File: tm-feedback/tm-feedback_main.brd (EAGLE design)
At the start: 100 x 80 mm, 38 parts

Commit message: Started on PIC schematic
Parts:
- added MICROCONTROLLER1:C2, MICROCONTROLLER1:C4, MICROCONTROLLER1:C5: 0.1uF, rcl:C0805
- added MICROCONTROLLER1:C3: 10uF, rcl:C0805
- added MICROCONTROLLER1:C6, MICROCONTROLLER1:C7: 27pF, rcl:C0805
- added MICROCONTROLLER1:LED2, MICROCONTROLLER1:LED3, MICROCONTROLLER1:LED4: (no value), led:CHIPLED_0805
- added MICROCONTROLLER1:R2, MICROCONTROLLER1:R3, MICROCONTROLLER1:R4, MICROCONTROLLER1:R5, MICROCONTROLLER1:R6: (no value), resistor:R0805
- added MICROCONTROLLER1:SJ1: (no value), jumper:SJ
- added MICROCONTROLLER1:U2: MCRSD20000F183000RR, tactile-music:CRYSTAL-FOOTPRINT
- moved MICROCONTROLLER1:LED1 289.0 mm to (-92.7, -359.4)
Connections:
- removed net MICROCONTROLLER1:AVDD: MICROCONTROLLER1:U1.17
- removed net MICROCONTROLLER1:AVSS: MICROCONTROLLER1:U1.16
- removed net MICROCONTROLLER1:VSS: MICROCONTROLLER1:U1.6
- new net MICROCONTROLLER1:!MCLR: MICROCONTROLLER1:JP1.6, MICROCONTROLLER1:R1.1, MICROCONTROLLER1:R2.1, MICROCONTROLLER1:SJ1.1
- new net MICROCONTROLLER1:LED1: MICROCONTROLLER1:R6.2
- new net MICROCONTROLLER1:LED2: MICROCONTROLLER1:R3.2
- new net MICROCONTROLLER1:LED3: MICROCONTROLLER1:R4.2
- new net MICROCONTROLLER1:LED4: MICROCONTROLLER1:R5.2
- new net MICROCONTROLLER1:N$1: MICROCONTROLLER1:R1.2, MICROCONTROLLER1:U1.18
- new net MICROCONTROLLER1:N$10: MICROCONTROLLER1:LED1.A, MICROCONTROLLER1:R6.1
- new net MICROCONTROLLER1:N$2: MICROCONTROLLER1:C1.1, MICROCONTROLLER1:SJ1.2
- new net MICROCONTROLLER1:N$3: MICROCONTROLLER1:C3.1, MICROCONTROLLER1:U1.7
- new net MICROCONTROLLER1:N$4: MICROCONTROLLER1:LED2.A, MICROCONTROLLER1:R3.1
- new net MICROCONTROLLER1:N$6: MICROCONTROLLER1:LED3.A, MICROCONTROLLER1:R4.1
- new net MICROCONTROLLER1:N$8: MICROCONTROLLER1:LED4.A, MICROCONTROLLER1:R5.1
- new net MICROCONTROLLER1:OSC1: MICROCONTROLLER1:C6.1, MICROCONTROLLER1:U1.30, MICROCONTROLLER1:U2.1
- new net MICROCONTROLLER1:OSC2: MICROCONTROLLER1:C7.1, MICROCONTROLLER1:U1.31, MICROCONTROLLER1:U2.2
- new net MICROCONTROLLER1:PGC: MICROCONTROLLER1:JP1.2
- new net MICROCONTROLLER1:PGD: MICROCONTROLLER1:JP1.3
- net D_3V3: now also MICROCONTROLLER1:C2.1, MICROCONTROLLER1:C4.1, MICROCONTROLLER1:C5.1, MICROCONTROLLER1:JP1.5, MICROCONTROLLER1:R2.2, MICROCONTROLLER1:U1.17, MICROCONTROLLER1:U1.28, MICROCONTROLLER1:U1.40
- net D_GND: now also MICROCONTROLLER1:C1.2, MICROCONTROLLER1:C2.2, MICROCONTROLLER1:C3.2, MICROCONTROLLER1:C4.2, MICROCONTROLLER1:C5.2, MICROCONTROLLER1:C6.2, MICROCONTROLLER1:C7.2, MICROCONTROLLER1:JP1.4, MICROCONTROLLER1:LED1.C, MICROCONTROLLER1:LED2.C, MICROCONTROLLER1:LED3.C, MICROCONTROLLER1:LED4.C, MICROCONTROLLER1:U1.16, MICROCONTROLLER1:U1.29, MICROCONTROLLER1:U1.39, MICROCONTROLLER1:U1.6

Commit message: Change PS, add button, remove MOTOR_DRIVER
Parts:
- removed MOTOR_DRIVER1:JP1, MOTOR_DRIVER2:JP1: (no value), jumper:JP1
- removed MOTOR_DRIVER1:LED1, MOTOR_DRIVER2:LED1: (no value), led:CHIPLED_0805
- removed MOTOR_DRIVER1:MOTOR, MOTOR_DRIVER2:MOTOR: JST-SMD-2, tactile-music:JST-SMD-2
- removed MOTOR_DRIVER1:R1, MOTOR_DRIVER2:R1: 10k, rcl:R0805
- removed MOTOR_DRIVER1:R2, MOTOR_DRIVER2:R2: (no value), rcl:R0805
- removed MOTOR_DRIVER1:U$1, MOTOR_DRIVER2:U$1: PMF370XN, tactile-music:SOT323(SC-70)
- removed MOTOR_DRIVER1:U$2, MOTOR_DRIVER2:U$2: DB2S308, tactile-music:SOD-523
- removed POWER_SUPPLY1:U$2: MCP1824T-3302E/OT, tactile-music:SOT95P270X145-5N
- added MOTOR_DRIVERS, OFF-BOARD_POWER, POWER_SUPPLY1:BATTERY: JST-SMD-2, tactile-music:JST-SMD-2
- added POWER_SUPPLY1:C1, POWER_SUPPLY1:C2: (no value), rcl:C0805
- added POWER_SUPPLY1:R2: 60, resistor:R0805
- added POWER_SUPPLY1:U$3: PMF370XN, tactile-music:SOT323(SC-70)
- POWER_SUPPLY1:R1: value (none) -> 60
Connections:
- removed net A_3V3: MOTOR_DRIVER1:JP1.1, MOTOR_DRIVER1:MOTOR.1, MOTOR_DRIVER1:U$2.1, MOTOR_DRIVER2:JP1.1, MOTOR_DRIVER2:MOTOR.1, MOTOR_DRIVER2:U$2.1
- removed net A_GND: MOTOR_DRIVER1:R1.1, MOTOR_DRIVER1:U$1.2, MOTOR_DRIVER2:R1.1, MOTOR_DRIVER2:U$1.2
- removed net BUTTON1:VCC: BUTTON1:U1.5
- removed net D_3V3: BLUETOOTH1:C1.1, BLUETOOTH1:U$1.23, MICROCONTROLLER1:C2.1, MICROCONTROLLER1:C4.1, MICROCONTROLLER1:C5.1, MICROCONTROLLER1:JP1.5, MICROCONTROLLER1:R2.2, MICROCONTROLLER1:U1.17, MICROCONTROLLER1:U1.28, MICROCONTROLLER1:U1.40
- removed net D_GND: BLUETOOTH1:C1.2, BLUETOOTH1:LED1.C, BLUETOOTH1:LED2.C, BLUETOOTH1:LED3.C, BLUETOOTH1:R2.1, BLUETOOTH1:U$1.1, BLUETOOTH1:U$1.16, BLUETOOTH1:U$1.24, BLUETOOTH1:U$1.9, MICROCONTROLLER1:C1.2, MICROCONTROLLER1:C2.2, MICROCONTROLLER1:C3.2, MICROCONTROLLER1:C4.2, MICROCONTROLLER1:C5.2, MICROCONTROLLER1:C6.2, MICROCONTROLLER1:C7.2, MICROCONTROLLER1:JP1.4, MICROCONTROLLER1:LED1.C, MICROCONTROLLER1:LED2.C, MICROCONTROLLER1:LED3.C, MICROCONTROLLER1:LED4.C, MICROCONTROLLER1:U1.16, MICROCONTROLLER1:U1.29, MICROCONTROLLER1:U1.39, MICROCONTROLLER1:U1.6
- removed net MOTOR_DRIVER1:N$1: MOTOR_DRIVER1:MOTOR.2, MOTOR_DRIVER1:R2.1, MOTOR_DRIVER1:U$1.3, MOTOR_DRIVER1:U$2.2
- removed net MOTOR_DRIVER1:N$2: MOTOR_DRIVER1:JP1.2, MOTOR_DRIVER1:LED1.A
- removed net MOTOR_DRIVER1:N$3: MOTOR_DRIVER1:LED1.C, MOTOR_DRIVER1:R2.2
- removed net MOTOR_DRIVER2:N$1: MOTOR_DRIVER2:MOTOR.2, MOTOR_DRIVER2:R2.1, MOTOR_DRIVER2:U$1.3, MOTOR_DRIVER2:U$2.2
- removed net MOTOR_DRIVER2:N$2: MOTOR_DRIVER2:JP1.2, MOTOR_DRIVER2:LED1.A
- removed net MOTOR_DRIVER2:N$3: MOTOR_DRIVER2:LED1.C, MOTOR_DRIVER2:R2.2
- removed net N$15: MOTOR_DRIVER1:R1.2, MOTOR_DRIVER1:U$1.1
- removed net N$16: MOTOR_DRIVER2:R1.2, MOTOR_DRIVER2:U$1.1
- new net +3V3: BLUETOOTH1:C1.1, BLUETOOTH1:U$1.23, MICROCONTROLLER1:C2.1, MICROCONTROLLER1:C4.1, MICROCONTROLLER1:C5.1, MICROCONTROLLER1:JP1.5, MICROCONTROLLER1:R2.2, MICROCONTROLLER1:U1.17, MICROCONTROLLER1:U1.28, MICROCONTROLLER1:U1.40, POWER_SUPPLY1:C2.2, POWER_SUPPLY1:R2.2, POWER_SUPPLY1:U$1.3, POWER_SUPPLY1:U$1.5
- new net BUTTON1:+3V3: BUTTON1:R1.2, BUTTON1:U1.5
- new net BUTTON1:N$1: BUTTON1:R1.1, BUTTON1:R2.2, BUTTON1:U$1.2
- new net BUTTON1:N$2: BUTTON1:C1.2, BUTTON1:R2.1, BUTTON1:U$1.1, BUTTON1:U1.2
- new net GND: BLUETOOTH1:C1.2, BLUETOOTH1:LED1.C, BLUETOOTH1:LED2.C, BLUETOOTH1:LED3.C, BLUETOOTH1:R2.1, BLUETOOTH1:U$1.1, BLUETOOTH1:U$1.16, BLUETOOTH1:U$1.24, BLUETOOTH1:U$1.9, BUTTON1:C1.1, BUTTON1:U1.3, MICROCONTROLLER1:C1.2, MICROCONTROLLER1:C2.2, MICROCONTROLLER1:C3.2, MICROCONTROLLER1:C4.2, MICROCONTROLLER1:C5.2, MICROCONTROLLER1:C6.2, MICROCONTROLLER1:C7.2, MICROCONTROLLER1:JP1.4, MICROCONTROLLER1:LED1.C, MICROCONTROLLER1:LED2.C, MICROCONTROLLER1:LED3.C, MICROCONTROLLER1:LED4.C, MICROCONTROLLER1:U1.16, MICROCONTROLLER1:U1.29, MICROCONTROLLER1:U1.39, MICROCONTROLLER1:U1.6, OFF-BOARD_POWER.2, POWER_SUPPLY1:C1.1, POWER_SUPPLY1:C2.1, POWER_SUPPLY1:R1.1, POWER_SUPPLY1:U$1.2, POWER_SUPPLY1:U$3.3
- new net N$1: BUTTON1:U1.4
- new net N$3: MOTOR_DRIVERS.1
- new net N$4: MOTOR_DRIVERS.2
- new net N$5: OFF-BOARD_POWER.1, POWER_SUPPLY1:C1.2, POWER_SUPPLY1:LED1.A, POWER_SUPPLY1:U$1.1
- new net POWER_SUPPLY1:BATT_V+: POWER_SUPPLY1:BATTERY.2, POWER_SUPPLY1:U$3.1
- new net POWER_SUPPLY1:BATT_V-: POWER_SUPPLY1:BATTERY.1, POWER_SUPPLY1:U$3.2
- new net POWER_SUPPLY1:N$3: POWER_SUPPLY1:LED1.C, POWER_SUPPLY1:R1.2
- new net POWER_SUPPLY1:N$5: POWER_SUPPLY1:R2.1, POWER_SUPPLY1:U$1.4

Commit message: Add power switch
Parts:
- added POWER_SUPPLY1:POWER_SW: JS102011SAQN, tactile-music:JS102011SAQN
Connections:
- net N$5: now also POWER_SUPPLY1:POWER_SW.3
- net POWER_SUPPLY1:BATT_V+: now also POWER_SUPPLY1:POWER_SW.2
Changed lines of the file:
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@@
 <element name="POWER_SUPPLY1:C2" library="rcl" package="C0805" value="" x="-97.79" y="-421.64"/>
 <element name="POWER_SUPPLY1:R2" library="resistor" package="R0805" value="60" x="-97.79" y="-426.72"/>
+<element name="POWER_SUPPLY1:POWER_SW" library="tactile-music" package="JS102011SAQN" value="JS102011SAQN" x="-93.98" y="-436.88"/>
 </elements>
 <signals>
@@
 <contactref element="POWER_SUPPLY1:C1" pad="2"/>
 <contactref element="POWER_SUPPLY1:U$1" pad="1"/>
+<contactref element="POWER_SUPPLY1:POWER_SW" pad="3"/>
 <wire x1="-96.84" y1="-416.56" x2="-96.25" y2="-373.92" width="0" layer="19" extent="1-1"/>
+<wire x1="-91.48" y1="-435.38" x2="-96.84" y2="-416.56" width="0" layer="19" extent="1-1"/>
 <wire x1="-59.7916" y1="-138.7602" x2="-96.25" y2="-373.92" width="0" layer="19" extent="1-1"/>
 <wire x1="-16.51" y1="-63.28" x2="-59.7916" y2="-138.7602" width="0" layer="19" extent="1-1"/>
@@
 <contactref element="POWER_SUPPLY1:BATTERY" pad="2"/>
 <contactref element="POWER_SUPPLY1:U$3" pad="1"/>
+<contactref element="POWER_SUPPLY1:POWER_SW" pad="2"/>
 <wire x1="-94.25" y1="-394.24" x2="-94.2" y2="-408.32" width="0" layer="19" extent="1-1"/>
+<wire x1="-93.98" y1="-435.38" x2="-94.2" y2="-408.32" width="0" layer="19" extent="1-1"/>
 </signal>
 <signal name="POWER_SUPPLY1:BATT_V-">

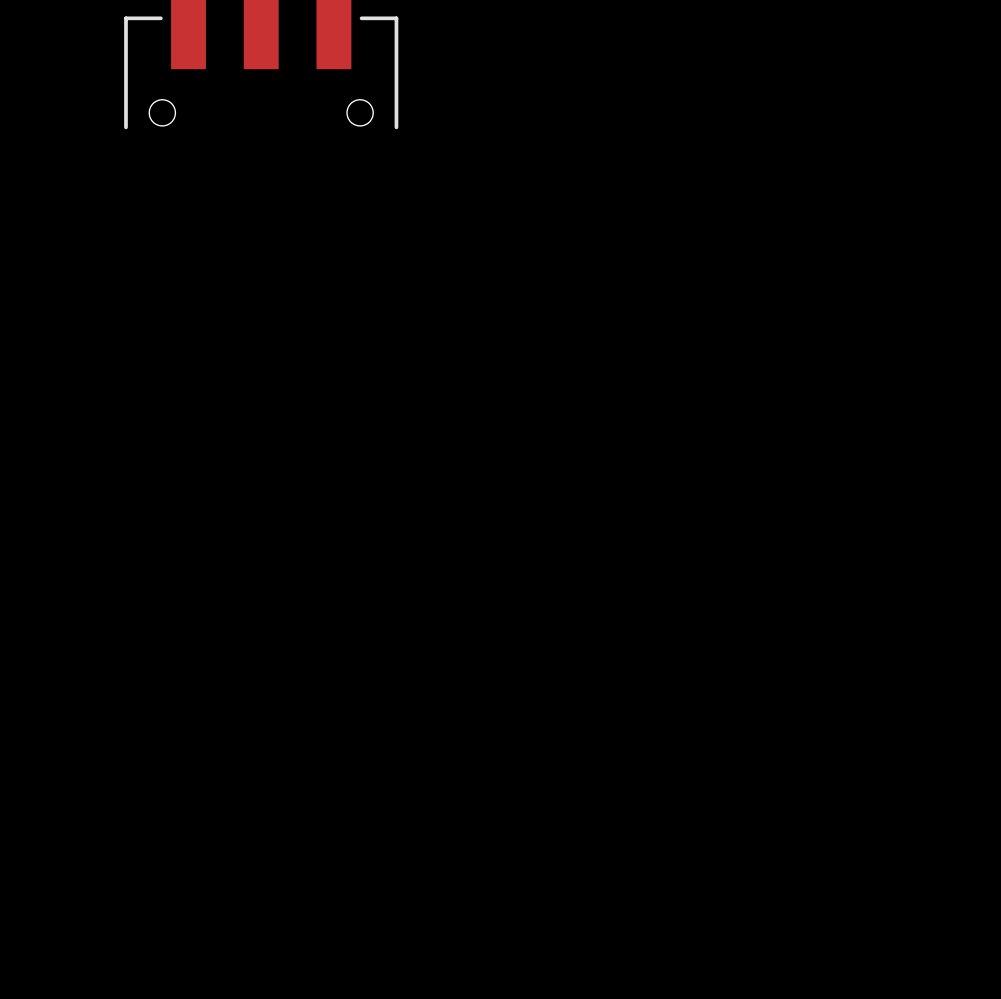
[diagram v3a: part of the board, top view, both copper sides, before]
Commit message: Wired most of the board up. Currently have ERC issues.
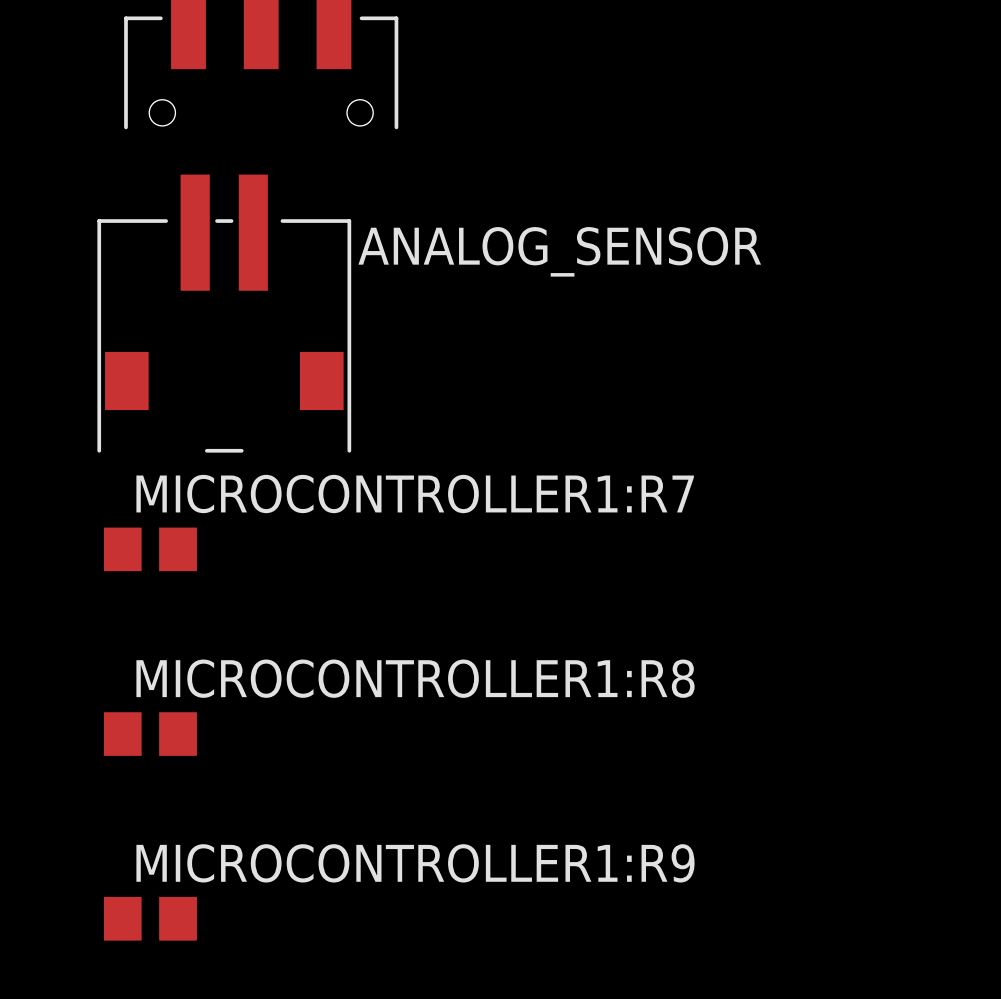
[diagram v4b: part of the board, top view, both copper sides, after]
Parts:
- added ANALOG_SENSOR: JST-SMD-2, tactile-music:JST-SMD-2
- added MICROCONTROLLER1:R7, MICROCONTROLLER1:R8, MICROCONTROLLER1:R9: 10kΩ, resistor:R0805
- BLUETOOTH1:LED1: value (none) -> BLUE
- BLUETOOTH1:LED2, MICROCONTROLLER1:LED1, MICROCONTROLLER1:LED3: value (none) -> GREEN
- BLUETOOTH1:LED3, MICROCONTROLLER1:LED2, MICROCONTROLLER1:LED4, POWER_SUPPLY1:LED1: value (none) -> RED
- BLUETOOTH1:R1, BLUETOOTH1:R3, BLUETOOTH1:R4, MICROCONTROLLER1:R4, MICROCONTROLLER1:R5, MICROCONTROLLER1:R6: value (none) -> 60Ω
- BLUETOOTH1:R2, MICROCONTROLLER1:R2: value (none) -> 10kΩ
- MICROCONTROLLER1:JP1: value (none) -> PICKIT
- MICROCONTROLLER1:JP2: value (none) -> UART_PC
- MICROCONTROLLER1:R1: value (none) -> 330Ω
- MICROCONTROLLER1:R3: value (none) -> 69Ω
- MICROCONTROLLER1:SJ1: value (none) -> MCLR_CAP
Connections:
- removed net BLUETOOTH1:CMD/MLDP: BLUETOOTH1:U$1.8
- removed net BLUETOOTH1:CONN: BLUETOOTH1:R3.2, BLUETOOTH1:U$1.10
- removed net BLUETOOTH1:MLDP_EV: BLUETOOTH1:R4.2, BLUETOOTH1:U$1.11
- removed net BLUETOOTH1:UART_CTS: BLUETOOTH1:U$1.14
- removed net BLUETOOTH1:UART_RTS: BLUETOOTH1:U$1.18
- removed net BLUETOOTH1:UART_RX: BLUETOOTH1:U$1.6
- removed net BLUETOOTH1:WAKE_HW: BLUETOOTH1:U$1.15
- removed net BLUETOOTH1:WAKE_SW: BLUETOOTH1:R2.2, BLUETOOTH1:U$1.7
- removed net BLUETOOTH1:WS: BLUETOOTH1:R1.2, BLUETOOTH1:U$1.12
- removed net BUTTON1:+3V3: BUTTON1:R1.2, BUTTON1:U1.5
- new net MICROCONTROLLER1:N$5: MICROCONTROLLER1:R7.1, MICROCONTROLLER1:U1.11, MICROCONTROLLER1:U1.12, MICROCONTROLLER1:U1.13, MICROCONTROLLER1:U1.14, MICROCONTROLLER1:U1.9
- new net MICROCONTROLLER1:N$7: MICROCONTROLLER1:R8.1, MICROCONTROLLER1:U1.25, MICROCONTROLLER1:U1.26
- new net MICROCONTROLLER1:N$9: MICROCONTROLLER1:R9.1, MICROCONTROLLER1:U1.32, MICROCONTROLLER1:U1.35
- new net MICROCONTROLLER1:UART2_RX: MICROCONTROLLER1:JP2.3, MICROCONTROLLER1:U1.33
- new net MICROCONTROLLER1:UART2_TX: MICROCONTROLLER1:JP2.2, MICROCONTROLLER1:U1.34
- new net N$10: BLUETOOTH1:R2.2, BLUETOOTH1:U$1.7, MICROCONTROLLER1:U1.3
- new net N$11: BLUETOOTH1:U$1.8, MICROCONTROLLER1:U1.2
- new net N$12: BLUETOOTH1:R3.2, BLUETOOTH1:U$1.10, MICROCONTROLLER1:U1.44
- new net N$13: BLUETOOTH1:R4.2, BLUETOOTH1:U$1.11, MICROCONTROLLER1:U1.43
- new net N$14: BLUETOOTH1:R1.2, BLUETOOTH1:U$1.12, MICROCONTROLLER1:U1.42
- new net N$15: ANALOG_SENSOR.1, MICROCONTROLLER1:U1.23
- new net N$16: ANALOG_SENSOR.2, MICROCONTROLLER1:U1.24
- new net N$6: BLUETOOTH1:U$1.18, MICROCONTROLLER1:U1.41
- new net N$7: BLUETOOTH1:U$1.5, MICROCONTROLLER1:U1.5
- new net N$8: BLUETOOTH1:U$1.6, MICROCONTROLLER1:U1.4
- new net N$9: BLUETOOTH1:U$1.15, MICROCONTROLLER1:U1.38
- net +3V3: now also BUTTON1:R1.2, BUTTON1:U1.5, MICROCONTROLLER1:JP2.4
- net GND: now also MICROCONTROLLER1:JP2.1, MICROCONTROLLER1:R7.2, MICROCONTROLLER1:R8.2, MICROCONTROLLER1:R9.2
- net MICROCONTROLLER1:LED1: now also MICROCONTROLLER1:U1.37
- net MICROCONTROLLER1:LED2: now also MICROCONTROLLER1:U1.1
- net MICROCONTROLLER1:LED3: now also MICROCONTROLLER1:U1.19
- net MICROCONTROLLER1:LED4: now also MICROCONTROLLER1:U1.20
- net MICROCONTROLLER1:PGC: now also MICROCONTROLLER1:U1.22
- net MICROCONTROLLER1:PGD: now also MICROCONTROLLER1:U1.21
- net N$1: now also MICROCONTROLLER1:U1.36
- net N$2: now also BLUETOOTH1:U$1.14, MICROCONTROLLER1:U1.27; no longer BLUETOOTH1:U$1.5
- net N$3: now also MICROCONTROLLER1:U1.10
- net N$4: now also MICROCONTROLLER1:U1.8
